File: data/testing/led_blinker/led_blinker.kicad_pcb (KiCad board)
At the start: 2 copper layers, 20 x 25 mm, 7 parts, among them U1 ATtiny85

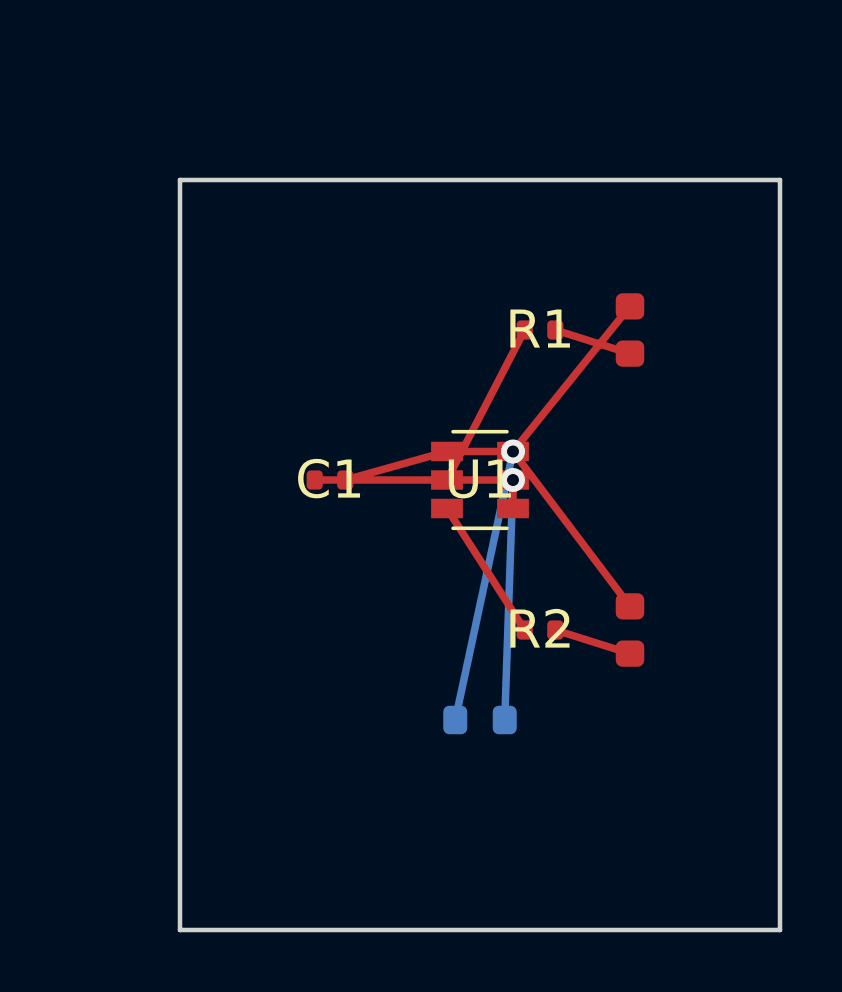
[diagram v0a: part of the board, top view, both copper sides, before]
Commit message: led blinkerのファイルを修正
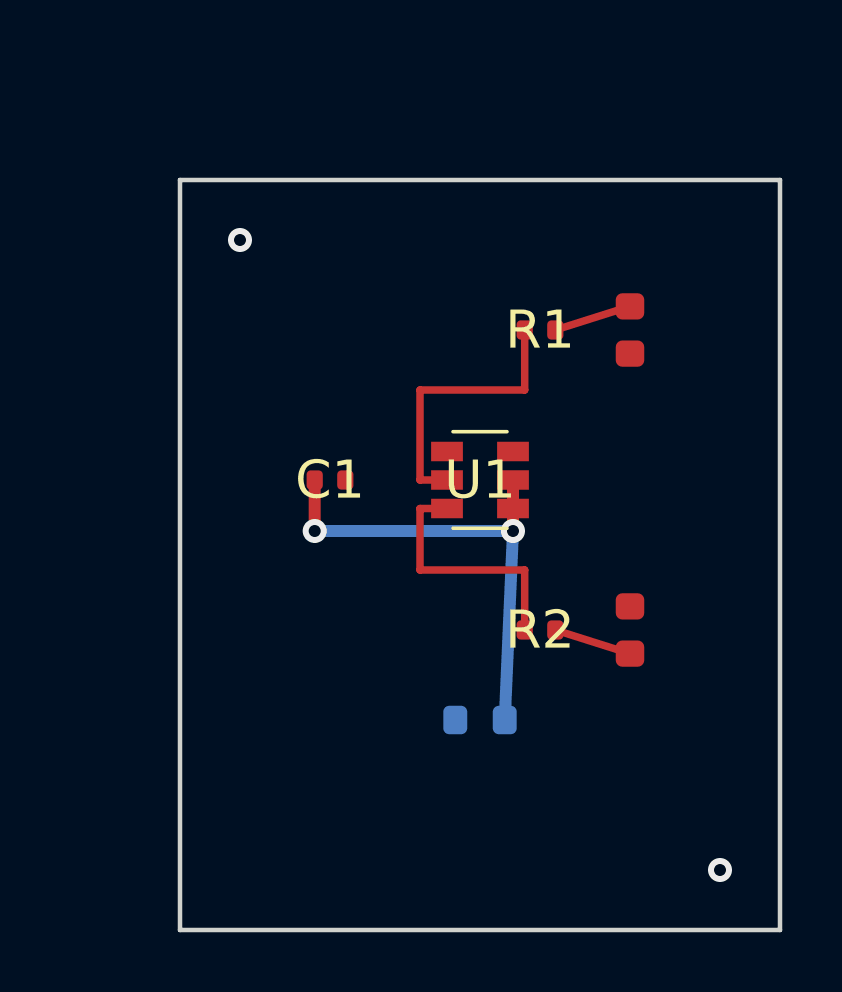
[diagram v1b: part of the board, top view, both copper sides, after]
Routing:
- net GND: track 27.6 -> 0.00 mm, vias 1 -> 2
- net LED1: track 8.24 -> 12.0 mm
- net LED2: track 7.42 -> 11.1 mm
- net VCC: track 15.6 -> 16.3 mm, vias 1 -> 2
- added copper zone on B.Cu, net GND
- added copper zone on F.Cu, net GND
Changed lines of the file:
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@@
 	)
 	(segment
-		(start 106.1 100.95)
-		(end 106.1 100)
-		(width 0.25)
-		(layer "F.Cu")
-		(net 1)
-	)
-	(segment
-		(start 106.1 100)
-		(end 99.49 100)
-		(width 0.25)
-		(layer "F.Cu")
-		(net 1)
-	)
-	(via
-		(at 106.1 100)
-		(size 0.8)
-		(drill 0.4)
-		(layers "F.Cu" "B.Cu")
-		(net 1)
-	)
-	(segment
-		(start 106.1 100)
-		(end 105.825 108)
-		(width 0.25)
-		(layer "B.Cu")
-		(net 1)
-	)
-	(segment
-		(start 103.9 99.05)
-		(end 106.1 99.05)
-		(width 0.25)
-		(layer "F.Cu")
-		(net 2)
-	)
-	(segment
-		(start 103.9 99.05)
-		(end 100.51 100)
-		(width 0.25)
-		(layer "F.Cu")
-		(net 2)
-	)
-	(segment
-		(start 106.1 99.05)
-		(end 110 94.2125)
-		(width 0.25)
-		(layer "F.Cu")
-		(net 2)
-	)
-	(segment
-		(start 106.1 99.05)
-		(end 110 104.2125)
-		(width 0.25)
-		(layer "F.Cu")
-		(net 2)
-	)
-	(via
-		(at 106.1 99.05)
-		(size 0.8)
-		(drill 0.4)
-		(layers "F.Cu" "B.Cu")
-		(net 2)
-	)
-	(segment
-		(start 106.1 99.05)
-		(end 104.175 108)
-		(width 0.25)
-		(layer "B.Cu")
-		(net 2)
-	)
-	(segment
-		(start 107.51 95)
-		(end 110 95.7875)
+		(start 103.9 100)
+		(end 103 100)
 		(width 0.25)
 		(layer "F.Cu")
@@
 	)
 	(segment
-		(start 103.9 100)
+		(start 103 100)
+		(end 103 97)
+		(width 0.25)
+		(layer "F.Cu")
+		(net 3)
+	)
+	(segment
+		(start 103 97)
+		(end 106.49 97)
+		(width 0.25)
+		(layer "F.Cu")
+		(net 3)
+	)
+	(segment
+		(start 106.49 97)
 		(end 106.49 95)
 		(width 0.25)
 		(layer "F.Cu")
 		(net 3)
+	)
+	(segment
+		(start 107.51 95)
+		(end 110 94.2125)
+		(width 0.25)
+		(layer "F.Cu")
+		(net 3)
+	)
+	(segment
+		(start 103.9 100.95)
+		(end 103 100.95)
+		(width 0.25)
+		(layer "F.Cu")
+		(net 4)
+	)
+	(segment
+		(start 103 100.95)
+		(end 103 103)
+		(width 0.25)
+		(layer "F.Cu")
+		(net 4)
+	)
+	(segment
+		(start 103 103)
+		(end 106.49 103)
+		(width 0.25)
+		(layer "F.Cu")
+		(net 4)
+	)
+	(segment
+		(start 106.49 103)
+		(end 106.49 105)
+		(width 0.25)
+		(layer "F.Cu")
+		(net 4)
 	)
 	(segment
@@
 	)
 	(segment
-		(start 103.9 100.95)
-		(end 106.49 105)
-		(width 0.25)
+		(start 106.1 100)
+		(end 106.1 101.7)
+		(width 0.4)
 		(layer "F.Cu")
-		(net 4)
+		(net 1)
+	)
+	(segment
+		(start 99.49 100)
+		(end 99.49 101.7)
+		(width 0.4)
+		(layer "F.Cu")
+		(net 1)
+	)
+	(via
+		(at 106.1 101.7)
+		(size 0.8)
+		(drill 0.4)
+		(layers "F.Cu" "B.Cu")
+		(net 1)
+	)
+	(via
+		(at 99.49 101.7)
+		(size 0.8)
+		(drill 0.4)
+		(layers "F.Cu" "B.Cu")
+		(net 1)
+	)
+	(segment
+		(start 99.49 101.7)
+		(end 106.1 101.7)
+		(width 0.4)
+		(layer "B.Cu")
+		(net 1)
+	)
+	(segment
+		(start 106.1 101.7)
+		(end 105.825 108)
+		(width 0.4)
+		(layer "B.Cu")
+		(net 1)
+	)
+	(via
+		(at 97 92)
+		(size 0.8)
+		(drill 0.4)
+		(layers "F.Cu" "B.Cu")
+		(net 2)
+	)
+	(via
+		(at 113 113)
+		(size 0.8)
+		(drill 0.4)
+		(layers "F.Cu" "B.Cu")
+		(net 2)
+	)
+	(zone
+		(net 2)
+		(net_name "GND")
+		(layer "F.Cu")
+		(name "GND_F")
+		(hatch edge 0.5)
+		(connect_pads
+			(clearance 0.5)
+		)
+		(min_thickness 0.25)
+		(filled_areas_thickness no)
+		(fill
+			(thermal_gap 0.5)
+			(thermal_bridge_width 0.5)
+		)
+		(polygon
+			(pts
+				(xy 95 90)
+				(xy 115 90)
+				(xy 115 115)
+				(xy 95 115)
+			)
+		)
+	)
+	(zone
+		(net 2)
+		(net_name "GND")
+		(layer "B.Cu")
+		(name "GND_B")
+		(hatch edge 0.5)
+		(connect_pads
+			(clearance 0.5)
+		)
+		(min_thickness 0.25)
+		(filled_areas_thickness no)
+		(fill
+			(thermal_gap 0.5)
+			(thermal_bridge_width 0.5)
+		)
+		(polygon
+			(pts
+				(xy 95 90)
+				(xy 115 90)
+				(xy 115 115)
+				(xy 95 115)
+			)
+		)
 	)
 	(embedded_fonts no)
